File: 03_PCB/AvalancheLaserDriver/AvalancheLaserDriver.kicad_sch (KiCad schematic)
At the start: 14 parts, among them J1 694106106102, J2 SMA, J3 Conn_01x02_Pin, J4 SMA, Q1 PJA3463_R1_00001

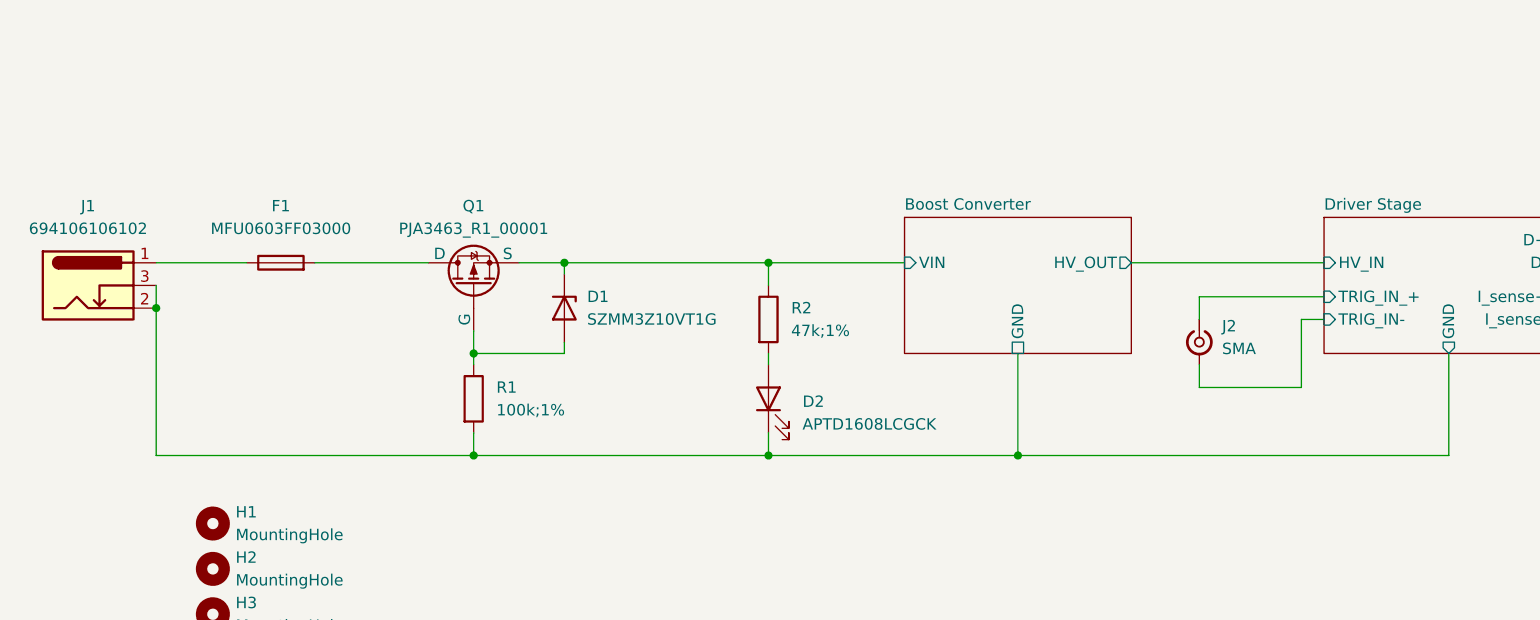
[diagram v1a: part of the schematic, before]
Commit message: feat(pcb): update laser driver circuit after first iteration
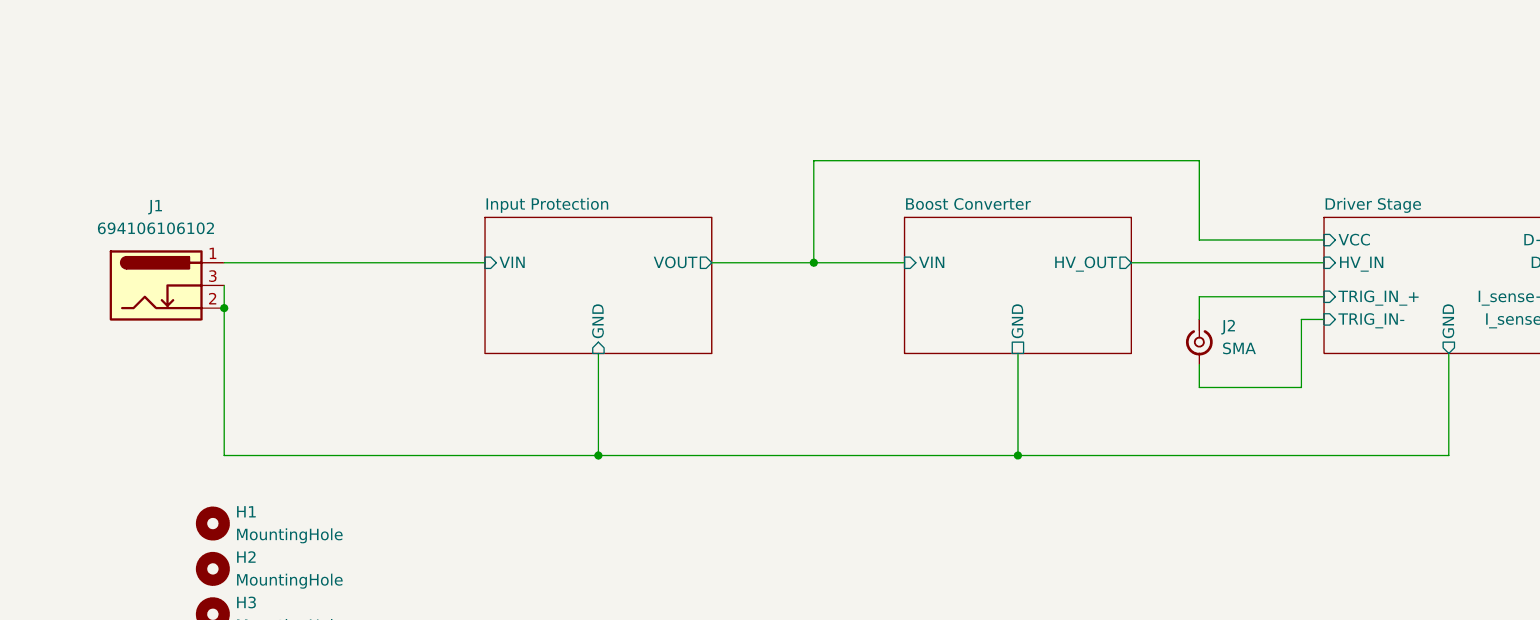
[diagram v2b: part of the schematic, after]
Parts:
- removed D1: SZMM3Z10VT1G, Diode_SMD:D_SOD-323, symbol Device:D_Zener
- removed D2: APTD1608LCGCK, LED_SMD:LED_0603_1608Metric, symbol Device:LED
- removed F1: MFU0603FF03000, Fuse:Fuse_0603_1608Metric, symbol Device:Fuse
- removed Q1: PJA3463_R1_00001, Package_TO_SOT_SMD:SOT-23, symbol Simulation_SPICE:PMOS
- removed R1: 100k;1%, Resistor_SMD:R_0603_1608Metric, symbol Device:R
- removed R2: 47k;1%, Resistor_SMD:R_0603_1608Metric, symbol Device:R
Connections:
- net Input Protection/VIN: now reaches J1.1
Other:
- added sheet Input Protection (InputProtection.kicad_sch)
- sheet Driver Stage ports: added VCC; removed none
- moved on the sheet: J1

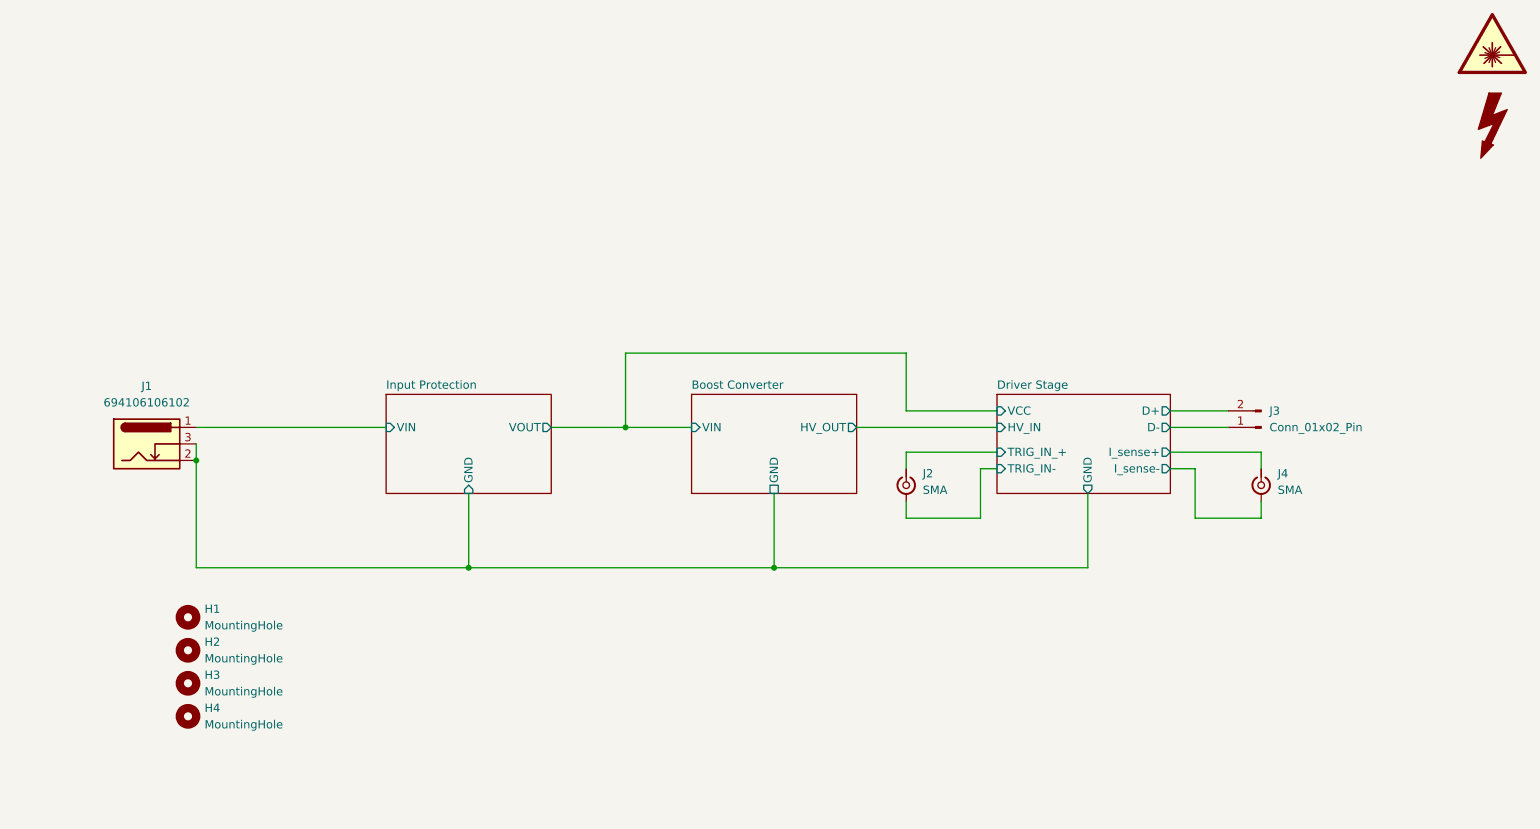
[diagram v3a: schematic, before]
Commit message: chore(pcb): update schematic with tuned component values and update notes
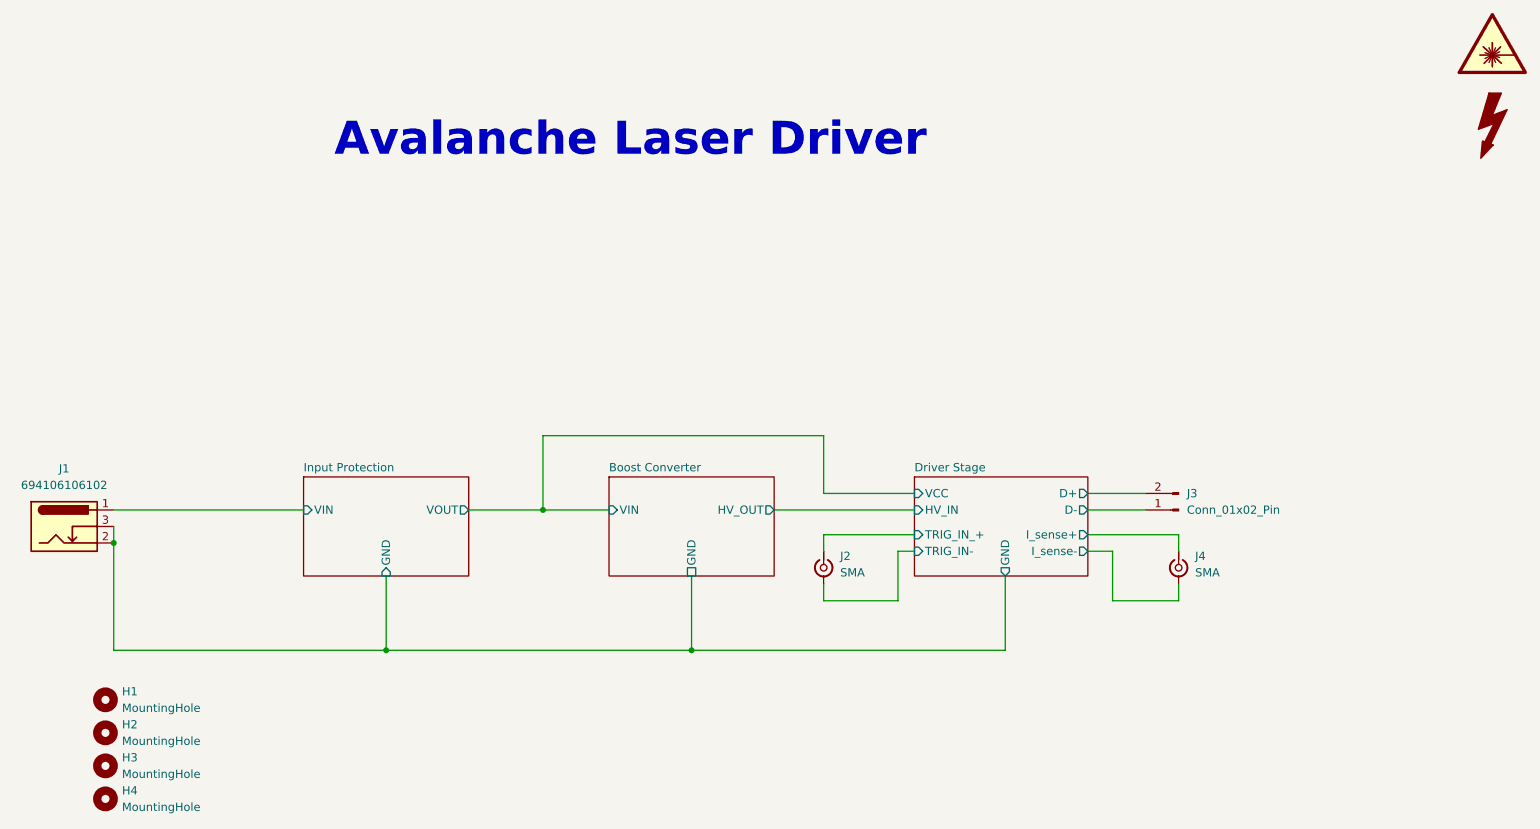
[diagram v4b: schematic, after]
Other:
- note added: "Avalanche Laser Driver"
- title: Lightspeed Laser Driver -> Avalanche Laser Driver
- moved on the sheet: H1, H2, H3, H4, J1, J2, J3, J4
